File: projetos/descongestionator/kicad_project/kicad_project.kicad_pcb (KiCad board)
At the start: 2 copper layers, 123 x 66.5 mm, 27 parts, among them J1 USB_A, J2 Conn_01x05_Socket, J3 U.FL-R-SMT_01_, Q1 PN2222A, U1 LCD-016N002L, U2 PCF8574, U3 CP2102N, U4 NEO-6M-GPS, U5 ATtiny202

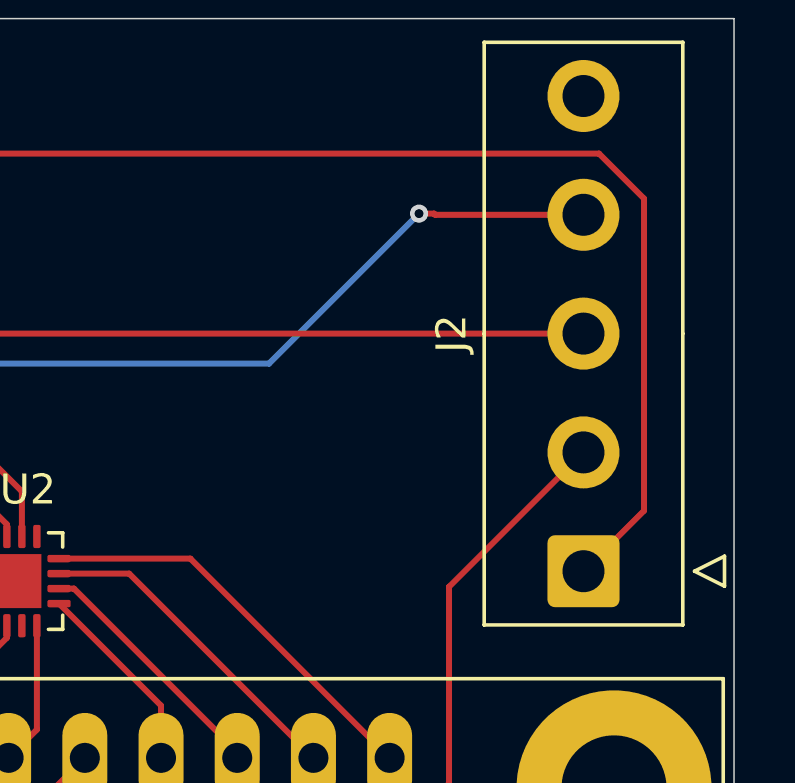
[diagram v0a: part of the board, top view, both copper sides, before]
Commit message: texto no conector da bússula
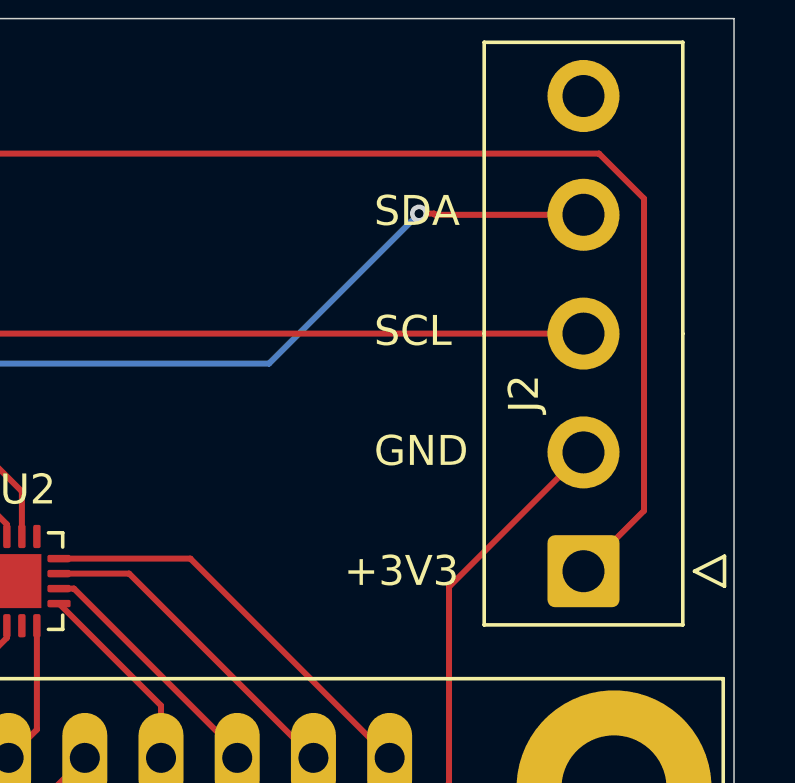
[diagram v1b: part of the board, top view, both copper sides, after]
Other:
- board text added: "+3V3"
- board text added: "GND"
- board text added: "SCL"
- board text added: "SDA"
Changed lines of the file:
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@@
 		(tags "connector TE 826576 vertical")
 		(property "Reference" "J2"
-			(at 7.92 -4.4 90)
+			(at 5.92 -1.9825 90)
 			(layer "F.SilkS")
 			(effects
@@
 		(layer "Edge.Cuts")
 	)
+	(gr_text "SDA"
+		(at 194 69 0)
+		(layer "F.SilkS")
+		(effects
+			(font
+				(size 1 1)
+				(thickness 0.1)
+			)
+			(justify left bottom)
+		)
+	)
+	(gr_text "+3V3"
+		(at 193 81 0)
+		(layer "F.SilkS")
+		(effects
+			(font
+				(size 1 1)
+				(thickness 0.1)
+			)
+			(justify left bottom)
+		)
+	)
+	(gr_text "GND"
+		(at 194 77 0)
+		(layer "F.SilkS")
+		(effects
+			(font
+				(size 1 1)
+				(thickness 0.1)
+			)
+			(justify left bottom)
+		)
+	)
+	(gr_text "SCL"
+		(at 194 73 0)
+		(layer "F.SilkS")
+		(effects
+			(font
+				(size 1 1)
+				(thickness 0.1)
+			)
+			(justify left bottom)
+		)
+	)
 	(gr_text "CaseTars"
